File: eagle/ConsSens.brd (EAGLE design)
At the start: 77.1 x 27.9 mm, 31 parts, among them Q3 12MHz, U3 3.3V, X1 MINI-USB-SHIELD-UX60A-MB-5ST

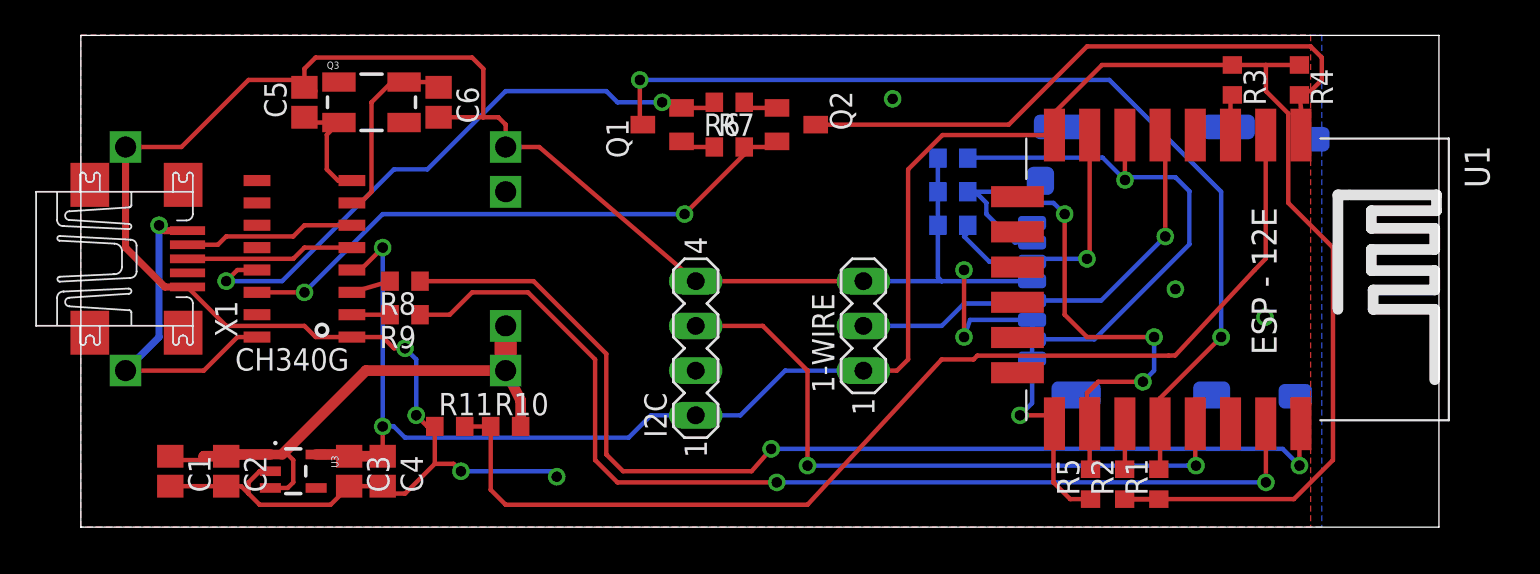
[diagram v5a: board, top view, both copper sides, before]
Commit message: New Micro-USB Connector
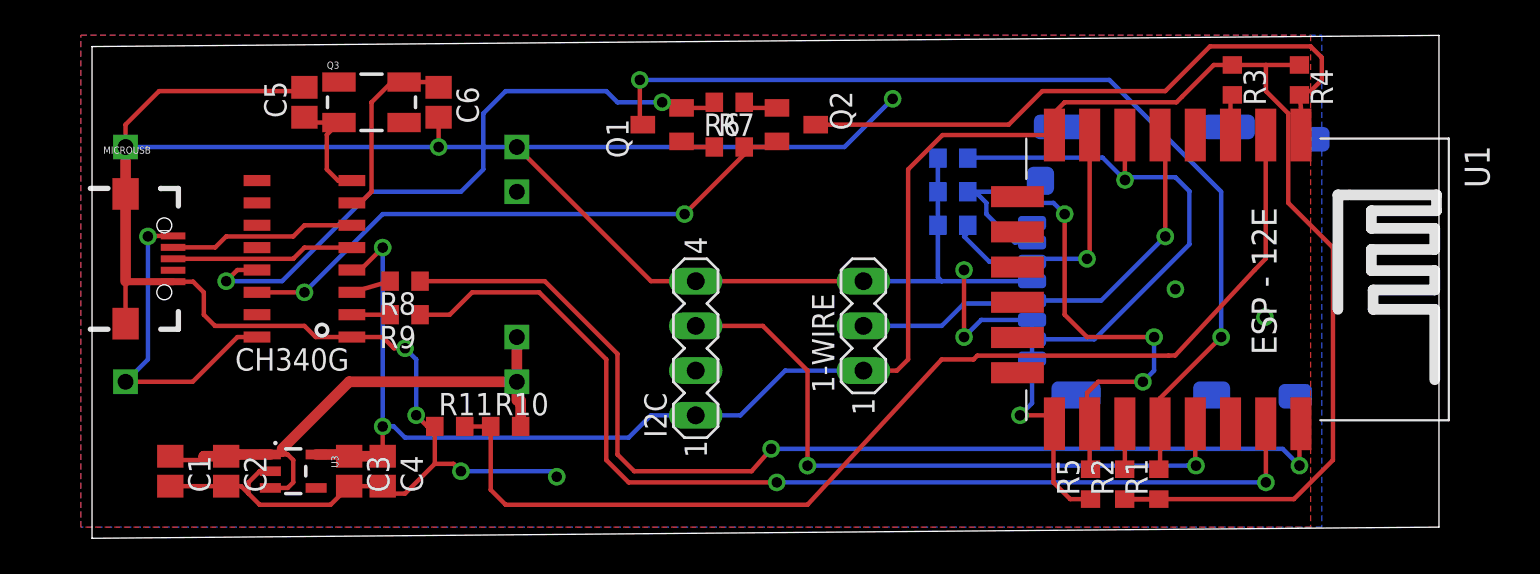
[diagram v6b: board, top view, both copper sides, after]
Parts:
- removed U$2: LIPOCHARGER, aliexpress:LIPOCHARGER
- removed X1: MINI-USB-SHIELD-UX60A-MB-5ST, con-hirose:UX60A-MB-5ST
- added MICROUSB: (no value), MicroUSB:USB-MICRO-SMD
- added U$4: TP4056-MODULE, userlib:TP4056-LITHIUM-PROTECTED-MODULE
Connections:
- new net B-: U$4.B-
- net GND: now also MICROUSB.GND1, U$4.IN-, U$4.OUT-; no longer U$2.IN-, U$2.OUT-, X1.5
- net N$5: now also MICROUSB.D-1; no longer X1.2
- net N$6: now also MICROUSB.D+1; no longer X1.3
- net OUT+: now also U$4.B+, U$4.OUT+; no longer U$2.B+, U$2.OUT+
- net USB5V: now also MICROUSB.VBUS1, U$4.IN+; no longer U$2.IN+, X1.1
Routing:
- net GND: track 153.4 -> 183.5 mm, vias 10 -> 11
- net N$4: track 34.7 -> 36.6 mm
- net N$5: track 9.79 -> 10.7 mm
- net N$6: track 9.60 -> 10.4 mm
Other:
- board size 77.1 x 27.9 mm -> 76.5 x 28.6 mm
